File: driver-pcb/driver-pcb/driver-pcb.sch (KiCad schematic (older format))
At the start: 1 part

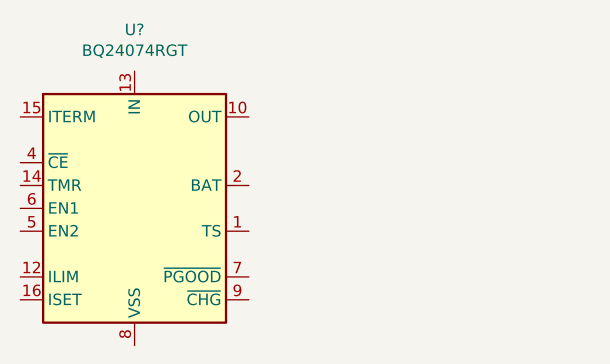
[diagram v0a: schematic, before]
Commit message: Schematic entered. Adding placing the resistors in the layout now.
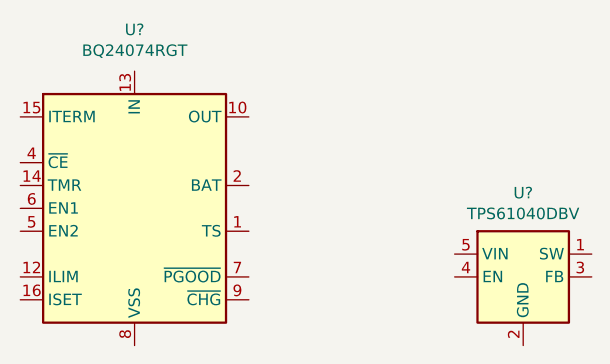
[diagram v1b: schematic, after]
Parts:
- added U?: TPS61040DBV, Package_TO_SOT_SMD:SOT-23-5, symbol Regulator_Switching:TPS61040DBV
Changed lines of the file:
@@
+	1    0    0    -1
+$EndComp
+$Comp
+L Regulator_Switching:TPS61040DBV U?
+U 1 1 5FE98D34
+P 3550 2600
+F 0 "U?" H 3550 2967 50  0000 C CNN
+F 1 "TPS61040DBV" H 3550 2876 50  0000 C CNN
+F 2 "Package_TO_SOT_SMD:SOT-23-5" H 3650 2350 50  0001 L CIN
+F 3 "http://www.ti.com/lit/ds/symlink/tps61040.pdf" H 3350 2900 50  0001 C CNN
+	1    3550 2600
 	1    0    0    -1
 $EndComp
